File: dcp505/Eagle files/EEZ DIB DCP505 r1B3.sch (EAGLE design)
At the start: 325 parts, among them IC1 LP2951, IC10 OPA4197IDR, IC11 MC33272ADR2G, IC12 MC33274ADR2G, IC13 74HC4066PW, IC14 74AUP1G74DC.125, IC15 MCP23S17-E/SS, IC16 REF5025AIDR, IC17 DAC8552IDGKR, IC18 SN74LVC1G3157DCKR, IC19 ADS1120IPWR, IC2 SI8641BB-B-IS1, IC20 LM339D, IC21 LM211PWR, IC3 SN74LVC1G139DCUR, IC4 MC79L05, IC5 SI8641BB-B-IS1, IC6 AT24C04D-SSHM-T, IC7 TMP1075AIDGK, IC8 TL072D, IC9 MC33274ADR2G, J1 FCR7350R, J2 FCR7350B, K1 G6K-2F-5DC, Q1 IRFP250MPBF, Q10 MMBT5551, Q11 PSMN0R9-25YLC, Q12 PSMN0R9-25YLC, Q13 PSMN0R9-25YLC, Q14 2N7002, Q15 2N7002, Q16 MMBT5401, Q17 MMBT5401, Q18 2N7002, Q19 BSS84P, Q2 BCP56-16.115, Q20 BTA26-600, Q21 2N7002, Q22 MMBT5551, Q23 2N7002, Q24 2N7002, Q25 MMBT5551, Q26 MMBT5551, Q27 MMBT5401, Q28 MMBT5551, Q29 MMBT5551, Q3 BC856C, Q30 BSS84P, Q31 2N7002, Q4 BCP56-16.115, Q5 STF10P6F6, Q6 BCP56-16.115, Q7 MMBT5401, Q8 MMBT5401, Q9 MMBT5551, X1 ZL263-26DG, X2 22-05-7085, X3 39-30-3035, X4 1844249, X5 ZL263-20DG

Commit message: #26, #28, #29
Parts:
- added C76: 10n, rcl:C-EUC0805
- added Q32: 2N7002, EEZ_Lib1:2N7002
- added R139: 10K, rcl:R-EU_R0805
- added R140: 470R, rcl:R-EU_R0805
- added R141: 100K, rcl:R-EU_R0805
- C11: value 470n -> 100n; device rcl:C-EUC0805 -> rcl:C-EUC0603
- C43: value 10n -> 47n; device rcl:C-EUC0603 -> rcl:C-EUC0805
- C44: device rcl:C-EUC0603 -> rcl:C-EUC0805
- C45: value 100n -> 10n; device rcl:C-EUC0603 -> rcl:C-EUC0805
- C47, C59, C61, C63: value 1u -> 100n; device rcl:C-EUC0805 -> rcl:C-EUC0603
- C48: value 10u -> 1u; device rcl:C-EUC1206 -> rcl:C-EUC0805
- C49: value 100n -> 10u; device rcl:C-EUC0603 -> rcl:C-EUC1206
- C50: value 4u7 -> 100n; device EEZ_Lib1:ECAP1206 -> rcl:C-EUC0603
- C51: value 1u -> 4u7; device rcl:C-EUC0805 -> EEZ_Lib1:ECAP1206
- C52, C60, C62, C64: value 100n -> 1u; device rcl:C-EUC0603 -> rcl:C-EUC0805
- C53: value 3n3 -> 100n; device rcl:C-EUC0805 -> rcl:C-EUC0603
- C55: value 10n -> 3n3
- C56: value 3n3 -> 10n
- C58: value 100n -> 3n3; device rcl:C-EUC0603 -> rcl:C-EUC0805
- C66, C68: value N.C. -> 100n; device rcl:C-EUC0805 -> rcl:C-EUC0603
- C67: value 100n -> 1n; device rcl:C-EUC0603 -> rcl:C-EUC0805
- C69: value 10n -> 1n
- C70: value 10n/200V -> 10n; device rcl:C-EUC1206 -> rcl:C-EUC0805
- C71: value 2n2 -> 10n/200V; device rcl:C-EUC0805 -> rcl:C-EUC1206
- C72: value 470n -> 2n2; device rcl:C-EUC1206 -> rcl:C-EUC0805
- C73: value HHXC630ARA330MHA0G -> 470n; device EEZ_Lib1:ECAPSMD8.3MM/HA0 -> rcl:C-EUC1206
- C74: value 10n/200V -> HHXC630ARA330MHA0G; device rcl:C-EUC1206 -> EEZ_Lib1:ECAPSMD8.3MM/HA0
- C75: value 10n -> 10n/200V; device rcl:C-EUC0805 -> rcl:C-EUC1206
- IC8: value TL072D -> MC33272ADR2G
- Q22: value MMBT5551 -> FMMT493TA
- Q25: value MMBT5551 -> 2N7002; device transistor:MMBT5551LT1-NPN-SOT23-BEC -> EEZ_Lib1:2N7002
- Q27: value MMBT5401 -> MMBT5551; device transistor:BC857B-PNP-SOT23-BEC -> transistor:MMBT5551LT1-NPN-SOT23-BEC
- Q28: value MMBT5551 -> MMBT5401; device transistor:MMBT5551LT1-NPN-SOT23-BEC -> transistor:BC857B-PNP-SOT23-BEC
- Q30: value BSS84P -> MMBT5551; device EEZ_Lib1:IRLML2246TRPBF -> transistor:MMBT5551LT1-NPN-SOT23-BEC
- Q31: value 2N7002 -> BSS84P; device EEZ_Lib1:2N7002 -> EEZ_Lib1:IRLML2246TRPBF; MPN 2N7002-7-F -> (none); OC_FARNELL 1713823 -> (none); OC_NEWARK 25R5679 -> (none); PACKAGE SOT-23-3 -> (none); SUPPLIER DIODES INC. -> (none)
- R100: value 10R -> 220R
- R101: value 10K -> 220R
- R102: value 10K -> 10R
- R103: value 470R -> 10K
- R104: value 5K1 -> 10K
- R105: value 47K -> 470R
- R106, R120: value 5K6 -> 5K1
- R107: value 330R -> 47K
- R108: value 750R -> 5K6
- R109, R114: value 1K -> 330R
- R110: value AC01000001007JA100 -> 750R; device rcl:R-EU_0411/15 -> rcl:R-EU_R0805
- R111: value 2K2 -> 1K
- R112: value 330R -> AC01000001007JA100; device rcl:R-EU_R0805 -> rcl:R-EU_0411/15
- R113: value 10K -> 2K2
- R116: value 6R8 -> 10K
- R117, R93: value 10K -> 100K
- R118: value 5K1 -> 6R2
- R122: value 1K -> 4K7
- R123: value 330R -> 5K6
- R124, R133: value 47K -> 10K
- R125: value 47K -> 1K
- R126: value 750R -> 330R
- R127: value 1K -> 47K
- R128: value 2K2 -> 47K
- R129: value 10K -> 750R
- R130, R77, R79, R84: value 10K -> 1K
- R131: value 1R -> 2K2
- R132: value 750R -> 10K
- R134: value 330R -> 1R
- R135: value 470R -> 750R
- R136: value 10K -> 47K
- R137: value 470R -> 330R
- R138: value 100K -> 470R
- R3: value 82K -> 86K6
- R59, R70: value 499K 0.1% -> 10K; device rcl:R-EU_R0603 -> rcl:R-EU_R0805
- R60: value 10K -> 1R
- R61: value 1R -> 0R1; device rcl:R-EU_R0805 -> rcl:R-EU_R1206
- R62: value 0R1 -> 0R010; device rcl:R-EU_R1206 -> EEZ_Lib1:R-EU_4WIREH2728
- R63: value 0R010 -> 10K; device EEZ_Lib1:R-EU_4WIREH2728 -> rcl:R-EU_R0805
- R64, R74: value 10K -> 499K 0.1%; device rcl:R-EU_R0805 -> rcl:R-EU_R0603
- R65: value 1K 0.1% -> 1K; device rcl:R-EU_R0603 -> rcl:R-EU_R0805
- R68: value 1K -> 40K2 0.1%; device rcl:R-EU_R0805 -> rcl:R-EU_R0603
- R69: value 40K2 0.1% -> 10K; device rcl:R-EU_R0603 -> rcl:R-EU_R0805
- R72: value 10K -> 0R010; device rcl:R-EU_R0805 -> EEZ_Lib1:R-EU_4WIREH2728
- R73: value 0R010 -> 1K 0.1%; device EEZ_Lib1:R-EU_4WIREH2728 -> rcl:R-EU_R0603
- R75, R81: value 100R -> 10K
- R76, R86: value 1K -> 1M
- R78, R82: value 1K -> 100R
- R88: value 100K -> 1K
- R89: value 270R -> 10K
- R90: value 47K -> 100K
- R91: value 100K -> 270R
- R92: value 470R -> 47K
- R94, R98, R99: value 220R -> 470R
- R95: value 220R -> 10K
- R96, R97: value 470R -> 220R
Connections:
- new net !OVP_FAULT: D23.C, IC15.GPA4, Q25.D, R122.2
- net !DP_DRIVE: now also R95.1; no longer R93.1
- net !FAULT_OUT: now also Q31.S, R89.2; no longer Q30.S, R87.2
- net !OVP_EN: now also Q26.B; no longer Q25.B
- net !SET_DP: now also R93.2; no longer R91.2
- net +5V: now also C46.1, C47.2, C60.2, R106.2, R120.2, R132.2, R138.2, R139.1, R89.1, R93.1; no longer C45.1, C46.2, C58.2, R104.2, R118.2, R129.2, R135.2, R136.1, R87.1, R91.1
- net +VREF: now also C51.+, C53.2, C63.2, R81.2, R87.2; no longer C50.+, C52.2, C62.2, R78.2, R85.2
- net AUX_IN: now also C56.2, R98.1; no longer C55.2, R96.1
- net AUX_USET_SW: now also R92.2; no longer R90.2
- net CC_ACTIVE: now also R120.1, R123.2; no longer R118.1, R120.2
- net CC_LED: now also R114.2; no longer R112.2
- net CV_ACTIVE: now also R106.1, R108.2; no longer R104.1, R106.2
- net CV_LED: now also R109.1; no longer R107.1
- net DP_LED: now also R95.2; no longer R93.2
- net GND: now also C46.2, C47.1, C49.2, C50.1, C51.-, C52.2, C56.1, C57.2, C63.1, C64.2, C69.1, Q25.S, Q27.E, Q29.E, Q31.D, Q32.S, R113.1, R115.2, R116.2, R117.1, R118.1, R119.2, R125.2, R127.1, R136.1, R141.1, R68.1, R71.1, R74.2, R91.2, R94.1; no longer C45.2, C46.1, C47.2, C49.1, C50.-, C51.2, C52.1, C56.2, C57.1, C63.2, C64.1, Q26.E, Q28.E, Q30.D, Q31.S, R111.1, R113.2, R114.2, R115.1, R116.1, R117.2, R122.2, R124.1, R133.1, R138.1, R69.1, R70.2, R72.1, R86.1, R89.2
- net ISENSE-: now also R68.2; no longer R69.2
- net I_CTRL: now also R59.2; no longer R60.2
- net I_MON: now also R101.1; no longer R99.1
- net I_SERVO: now also R124.1; no longer R121.1
- net I_SET: now also R96.1; no longer R94.1
- net N$1: now also R67.2, R72.2S; no longer R65.2, R73.2S
- net N$105: now also R108.1; no longer R106.1
- net N$106: now also R123.1; no longer R120.1
- net N$107: now also C70.2, Q28.B, R126.1, R129.2, R131.2; no longer C69.2, Q27.B, R123.1, R126.2, R128.2
- net N$108: now also C72.2, Q28.C, R128.1, R133.2; no longer C71.2, Q27.C, R125.1, R130.2
- net N$109: now also Q30.C, R130.1; no longer Q29.C, R127.1
- net N$110: now also C76.1, Q30.B, R135.1, R137.2; no longer C75.1, Q29.B, R132.1, R134.2
- net N$111: now also C72.1, Q27.B, R127.2, R128.2; no longer C71.1, Q26.B, R124.2, R125.2
- net N$112: now also Q29.B, R133.1, R136.2; no longer Q28.B, R130.1, R133.2
- net N$113: now also C73.2, R134.2; no longer C72.2, R131.2
- net N$114: now also Q32.D, R140.1; no longer Q31.D, R137.1
- net N$118: now also R109.2; no longer R107.2
- net N$12: now also R91.1; no longer R89.1
- net N$120: now also R140.2; no longer R137.2
- net N$121: now also R94.2; no longer R92.2
- net N$14: now also Q31.G, R139.2; no longer Q30.G, R136.2
- net N$15: now also R112.2; no longer R110.2
- net N$153: now also R103.2; no longer R101.2
- net N$161: now also R124.2; no longer R121.2
- net N$17: now also R98.2, R99.1; no longer R96.2, R97.1
- net N$170: now also R107.1, R113.2; no longer R105.1, R111.2
- net N$173: now also R130.2, R131.1; no longer R127.2, R128.1
- net N$177: now also R119.1, R121.2; no longer R117.1, R119.2
- net N$18: now also R105.1; no longer R103.1
- net N$19: now also R118.2; no longer R116.2
- net N$21: now also R111.1, R117.2; no longer R109.1, R115.2
- net N$23: now also R85.2, R87.1; no longer R83.2, R85.1
- net N$24: now also Q26.C; no longer Q25.C
- net N$25: now also R138.1; no longer R135.1
- net N$28: now also C43.1, R64.2, R67.1; no longer R59.2, R65.1
- net N$29: now also R62.2; no longer R63.2
- net N$30: now also Q26.E, R125.1; no longer Q25.E, R122.1
- net N$31: now also C67.2, R104.2; no longer C66.2, R102.2
- net N$32: now also R99.2; no longer R97.2
- net N$33: now also C69.2, R110.2, R115.1; no longer C68.2, R108.2, R113.1
- net N$35: now also C43.2, R64.1, R69.2; no longer R59.1, R74.2
- net N$37: now also C44.2, R76.1; no longer C43.2
- net N$4: now also C71.1, C73.1, C74.+, Q28.E, R126.2; no longer C69.1, C72.1, C73.+, Q27.E, R123.2
- net N$40: now also R63.1; no longer R64.1
- net N$41: now also R59.1, R63.2; no longer R60.1, R64.2
- net N$42: now also R79.1, R84.2; no longer R78.1, R82.2
- net N$43: now also C45.2, R65.2, R86.1; no longer C44.2, R68.2
- net N$44: now also R70.1, R71.2; no longer R71.1, R72.2
- net N$45: now also R90.2; no longer R88.2
- net N$46: now also R114.1; no longer R112.1
- net N$47: now also R84.1, R88.2; no longer R82.1, R86.2
- net N$48: now also R82.2, R85.1; no longer R81.2, R83.1
- net N$50: now also R72.1S, R73.2; no longer R67.2, R73.1S
- net N$51: now also R62.1S; no longer R63.1S
- net N$52: now also R77.2, R81.1; no longer R76.2, R79.1
- net N$53: now also R77.1, R78.2; no longer R75.2, R76.1
- net N$54: now also R73.1, R74.1; no longer R67.1, R70.1
- net N$56: now also R61.2; no longer R62.2
- net N$57: now also R69.1; no longer R74.1
- net N$58: now also R75.2, R78.1; no longer R75.1, R77.2
- net N$59: now also R62.2S; no longer R63.2S
- net N$62: now also R82.1, R83.2; no longer R81.1, R84.2
- net N$63: now also R60.1; no longer R61.1
- net N$65: now also C44.1, R75.1, R76.2; no longer C43.1, R77.1
- net N$67: now also C45.1, R83.1, R86.2; no longer C44.1, R84.1
- net N$7: now also D15.C, R60.2, R61.1, R72.2; no longer R61.2, R63.1, R73.2
- net N$70: now also C62.2, R102.2; no longer C60.2, R100.2
- net N$71: now also C52.1; no longer C51.1
- net N$72: now also C54.2, R96.2; no longer C53.2, R94.2
- net N$73: now also C58.2, R100.2; no longer C57.2, R98.2
- net N$74: now also R65.1; no longer R68.1
- net N$8: now also R70.2; no longer R71.2
- net N$80: now also C55.2, R97.2; no longer C54.2, R95.2
- net N$81: now also C57.1, R101.2; no longer C56.1, R99.2
- net OUTF+: now also R105.2; no longer R103.2
- net OVP_FAULT: now also Q25.G, R111.2, R116.1; no longer IC15.GPA4, R109.2, R114.1
- net PE: now also C71.2, C75.1; no longer C70.2, C74.1
- net POST_OUT-: now also C74.-, C76.2, Q30.E, R137.1; no longer C73.-, C74.2, Q29.E, R131.1
- net PREG_OUT-: now also R112.1, R72.1; no longer D15.C, R110.1, R73.1
- net PWRGOOD: no longer D23.C
- net RSENSE: now also Q32.G, R141.2; no longer Q31.G, R138.2
- net SENSE+: now also R129.1; no longer R126.1
- net SENSE-: now also R135.2; no longer R132.2
- net SENSE_ERR: now also Q29.C, R132.1; no longer Q28.C, R129.1
- net SENSE_PROT: now also Q27.C; no longer Q26.C
- net U_MON: now also R100.1, R110.1; no longer R108.1, R98.1
- net U_SERVO: now also R103.1; no longer R101.1
- net U_SET: now also R104.1, R97.1; no longer R102.1, R95.1
- net V+: now also C49.1, C50.2, C64.1, C66.2, IC12P.V+, R102.1, R107.2, R122.1; no longer C47.1, C49.2, C63.1, C64.2, IC12P.V-, R100.1, R105.2
- net V-: now also C68.2, IC12P.V-, R121.1; no longer C67.2, IC12P.V+, R119.1
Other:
- note added: "I_SET ranges: 0 - 0.833 V = CURR_50MA range 0.833 - 1.66 V = CURR_500MA range 1.66 - 2.5 V = CURR_5A range"
- note added: "Note 3.1: Use power resistors with the lowest possible TCR (below ± 50 ppm/oC), e.g. GMR100HTBFA10L0, CSSH2728FT10L0 or OARS1 - R010FI"
- note added: "R29, R38"
- note added: "R30, R39"
- note removed: "I_SET (+2.5 V for full range)"
- note removed: "Note 3.1: Use power resistors with the lowest possible TCR (± 50 ppm/oC or better), e.g. CRA2512-FZ-R020ELF"
- note removed: "R96, R105"
- note removed: "R97, R106"
- moved on the sheet: C43, C44, C46, C47, C48, C49, C52, C53, C54, C55, C56, C57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

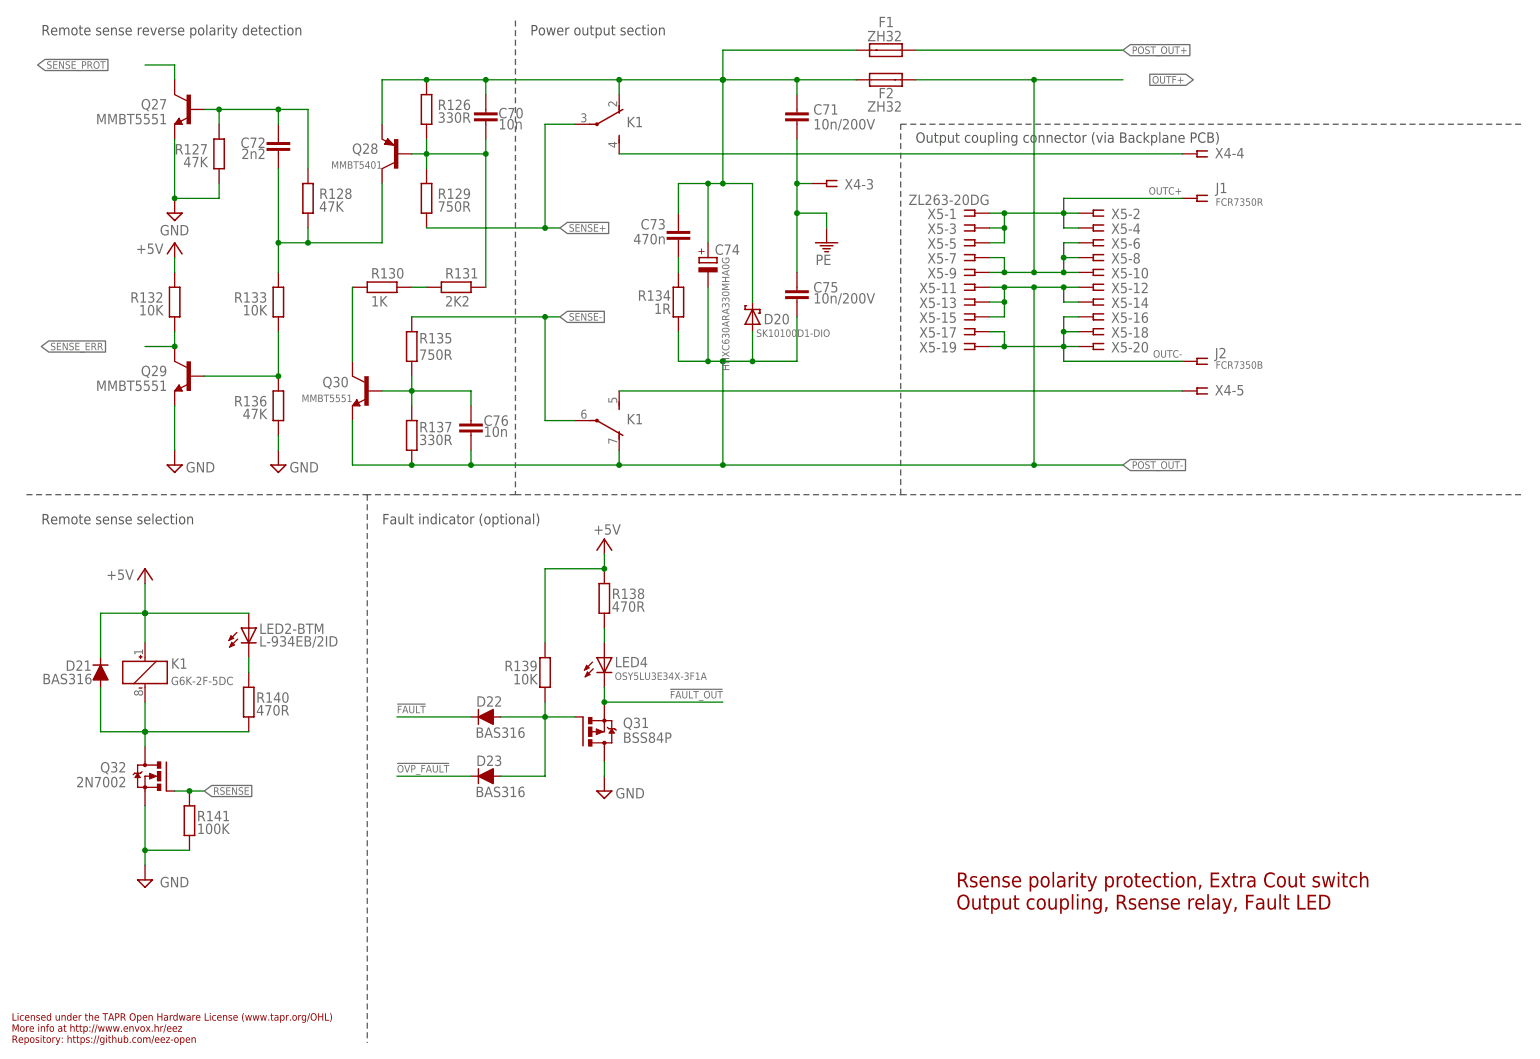
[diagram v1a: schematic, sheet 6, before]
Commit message: DCP505 fault indication fix
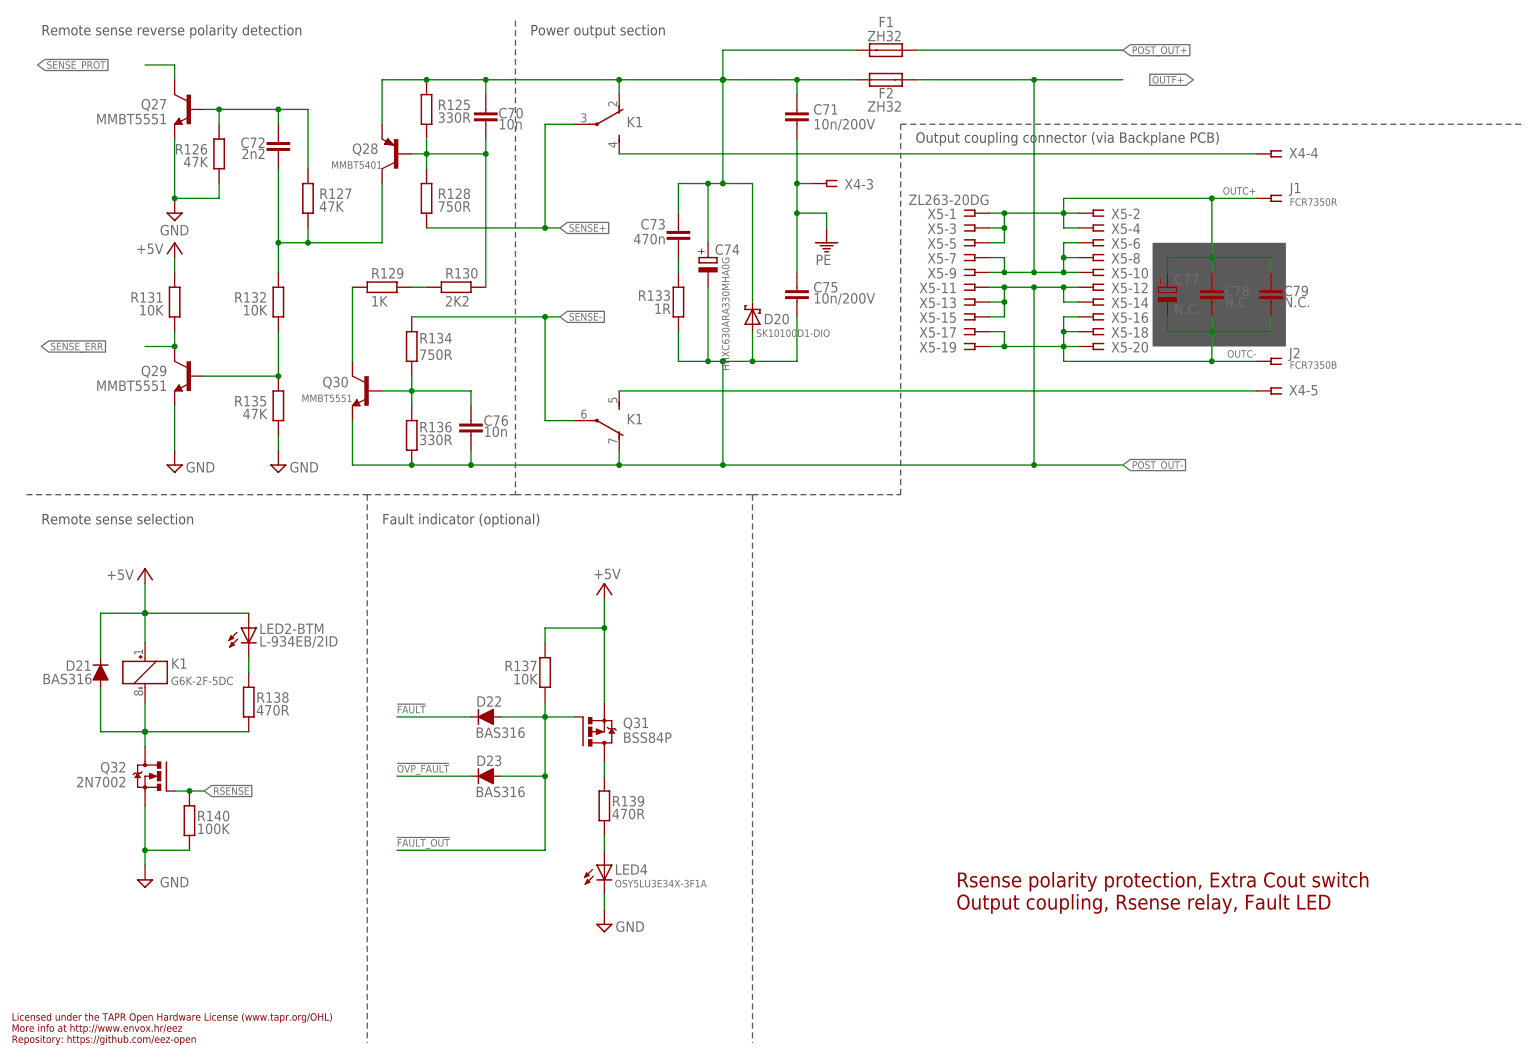
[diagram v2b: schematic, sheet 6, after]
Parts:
- removed R141: 100K, rcl:R-EU_R0805
- added C77: N.C., EEZ_Lib1:ECAP2G/5
- added C78, C79: N.C., rcl:C-EUC0805
- R101: value 220R -> 10R
- R102: value 10R -> 10K
- R104, R139: value 10K -> 470R
- R105: value 470R -> 5K1
- R106: value 5K1 -> 47K
- R107: value 47K -> 5K6
- R108: value 5K6 -> 330R
- R109: value 330R -> 750R
- R110, R129: value 750R -> 1K
- R111: value 1K -> AC01000001007JA100; device rcl:R-EU_R0805 -> rcl:R-EU_0411/15
- R112: value AC01000001007JA100 -> 2K2; device rcl:R-EU_0411/15 -> rcl:R-EU_R0805
- R113: value 2K2 -> 330R
- R114, R137: value 330R -> 10K
- R116, R89: value 10K -> 100K
- R117: value 100K -> 6R2
- R118: value 6R2 -> 10K
- R119: value 10K -> 5K1
- R120: value 5K1 -> 10K
- R121: value 10K -> 4K7
- R122: value 4K7 -> 5K6
- R123: value 5K6 -> 10K
- R124: value 10K -> 1K
- R125: value 1K -> 330R
- R126: value 330R -> 47K
- R128: value 47K -> 750R
- R130: value 1K -> 2K2
- R131: value 2K2 -> 10K
- R133: value 10K -> 1R
- R134: value 1R -> 750R
- R135: value 750R -> 47K
- R136: value 47K -> 330R
- R140: value 470R -> 100K
- R3: value 86K6 -> 82K
- R51: device rcl:R-EU_R0805 -> rcl:R-EU_R0603
- R90: value 100K -> 270R
- R91: value 270R -> 47K
- R92: value 47K -> 100K
- R93: value 100K -> 470R
- R94: value 470R -> 10K
- R95: value 10K -> 220R
- R97: value 220R -> 470R
- R99: value 470R -> 220R
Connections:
- net N$16 renamed U_CTRL+
- net N$27 renamed U_CTRL-
- removed net N$14: D22.A, D23.A, Q31.G, R139.2
- new net N$16: LED4.A, R139.1
- net !DP_DRIVE: now also R94.1; no longer R95.1
- net !FAULT_OUT: now also D22.A, D23.A, Q31.G, R137.2; no longer LED4.C, Q31.S, R89.2
- net !OVP_FAULT: now also R121.2; no longer R122.2
- net !SET_DP: now also R92.2; no longer R93.2
- net +5V: now also Q31.S, R105.2, R119.2, R131.2, R137.1, R92.1; no longer R106.2, R120.2, R132.2, R138.2, R139.1, R89.1, R93.1
- net AUX_IN: now also R97.1; no longer R98.1
- net AUX_USET_SW: now also R91.2; no longer R92.2
- net CC_ACTIVE: now also R119.1, R122.2; no longer R120.1, R123.2
- net CC_LED: now also R113.2; no longer R114.2
- net CV_ACTIVE: now also R105.1, R107.2; no longer R106.1, R108.2
- net CV_LED: now also R108.1; no longer R109.1
- net DP_LED: now also R94.2; no longer R95.2
- net GND: now also LED4.C, R112.1, R114.2, R116.1, R118.2, R124.2, R126.1, R135.1, R140.1, R89.1, R90.2, R91.1, R93.1; no longer Q31.D, R113.1, R116.2, R118.1, R119.2, R125.2, R127.1, R136.1, R141.1, R90.1, R91.2, R92.1, R94.1
- net I_MON: now also R100.1; no longer R101.1
- net I_SERVO: now also R123.1; no longer R124.1
- net I_SET: now also R95.1; no longer R96.1
- net N$105: now also R107.1; no longer R108.1
- net N$106: now also R122.1; no longer R123.1
- net N$107: now also R125.1, R128.2, R130.2; no longer R126.1, R129.2, R131.2
- net N$108: now also R127.1, R132.2; no longer R128.1, R133.2
- net N$109: now also R129.1; no longer R130.1
- net N$110: now also R134.1, R136.2; no longer R135.1, R137.2
- net N$111: now also R126.2; no longer R128.2
- net N$112: now also R132.1, R135.2; no longer R133.1, R136.2
- net N$113: now also R133.2; no longer R134.2
- net N$114: now also R138.1; no longer R140.1
- net N$118: now also R108.2; no longer R109.2
- net N$12: now also R90.1; no longer R91.1
- net N$120: now also R138.2; no longer R140.2
- net N$121: now also R93.2; no longer R94.2
- net N$15: now also R111.2; no longer R112.2
- net N$153: now also R102.2; no longer R103.2
- net N$161: now also R123.2; no longer R124.2
- net N$17: now also R97.2, R98.1; no longer R98.2, R99.1
- net N$170: now also R106.1, R112.2; no longer R107.1, R113.2
- net N$173: now also R129.2, R130.1; no longer R130.2, R131.1
- net N$177: now also R118.1, R120.2; no longer R119.1, R121.2
- net N$18: now also R104.1; no longer R105.1
- net N$19: now also R117.2; no longer R118.2
- net N$21: now also R110.1, R116.2; no longer R111.1, R117.2
- net N$25: now also Q31.D, R139.2; no longer LED4.A, R138.1
- net N$30: now also R124.1; no longer R125.1
- net N$31: now also R103.2; no longer R104.2
- net N$32: now also R98.2; no longer R99.2
- net N$33: now also R109.2, R114.1; no longer R110.2, R115.1
- net N$4: now also R125.2; no longer R126.2
- net N$45: now also R89.2; no longer R90.2
- net N$46: now also R113.1; no longer R114.1
- net N$70: now also R101.2; no longer R102.2
- net N$72: now also R95.2; no longer R96.2
- net N$73: now also R99.2; no longer R100.2
- net N$80: now also R96.2; no longer R97.2
- net N$81: now also R100.2; no longer R101.2
- net OUTC+: now also C77.+, C78.1, C79.1
- net OUTC-: now also C77.-, C78.2, C79.2
- net OUTF+: now also R104.2; no longer R105.2
- net OVP_FAULT: now also R110.2, R115.1; no longer R111.2, R116.1
- net POST_OUT-: now also R133.1, R136.1; no longer R134.1, R137.1
- net PREG_OUT-: now also R111.1; no longer R112.1
- net RSENSE: now also R140.2; no longer R141.2
- net SENSE+: now also R128.1; no longer R129.1
- net SENSE-: now also R134.2; no longer R135.2
- net SENSE_ERR: now also R131.1; no longer R132.1
- net U_MON: now also R109.1, R99.1; no longer R100.1, R110.1
- net U_SERVO: now also R102.1; no longer R103.1
- net U_SET: now also R103.1, R96.1; no longer R104.1, R97.1
- net V+: now also R101.1, R106.2, R121.1; no longer R102.1, R107.2, R122.1
- net V-: now also R120.1; no longer R121.1
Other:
- note added: "U_CTRL+ 5"
- note added: "U_CTRL- 6"
- note removed: "U_MON+ 5"
- note removed: "U_MON- 6"
- moved on the sheet: D17, J1, J2, LED4, R100, R101, R103, R104, R105, R106, R107, R108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
